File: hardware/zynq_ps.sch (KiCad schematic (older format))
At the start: 26 parts, among them J1801 DM3CS, SW1801 SW_Push, U1801 CAT24C02TDI-GT3, U1802 EMIF06-MSD02N16, U1803 33.333MHZ, U201 xc7z030sbg485

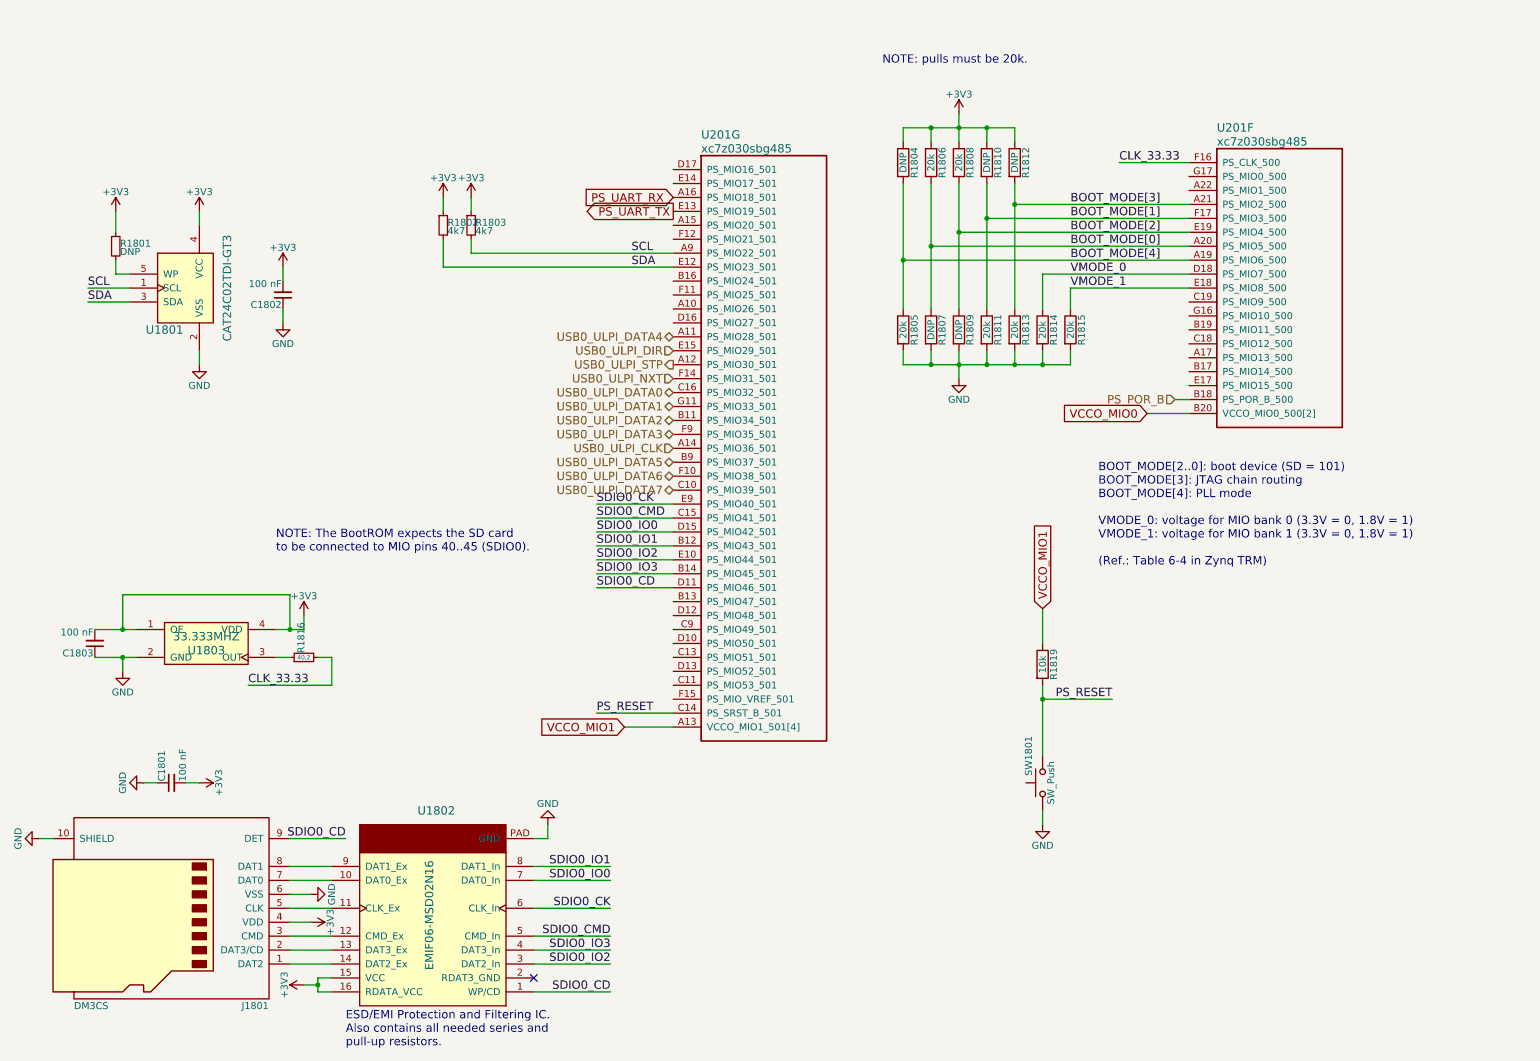
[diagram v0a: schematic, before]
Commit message: WIP: routing the HF Part of the Camera Connector. I have to move the clock away from the left border.
TODO: Fix DDR3 RAM.
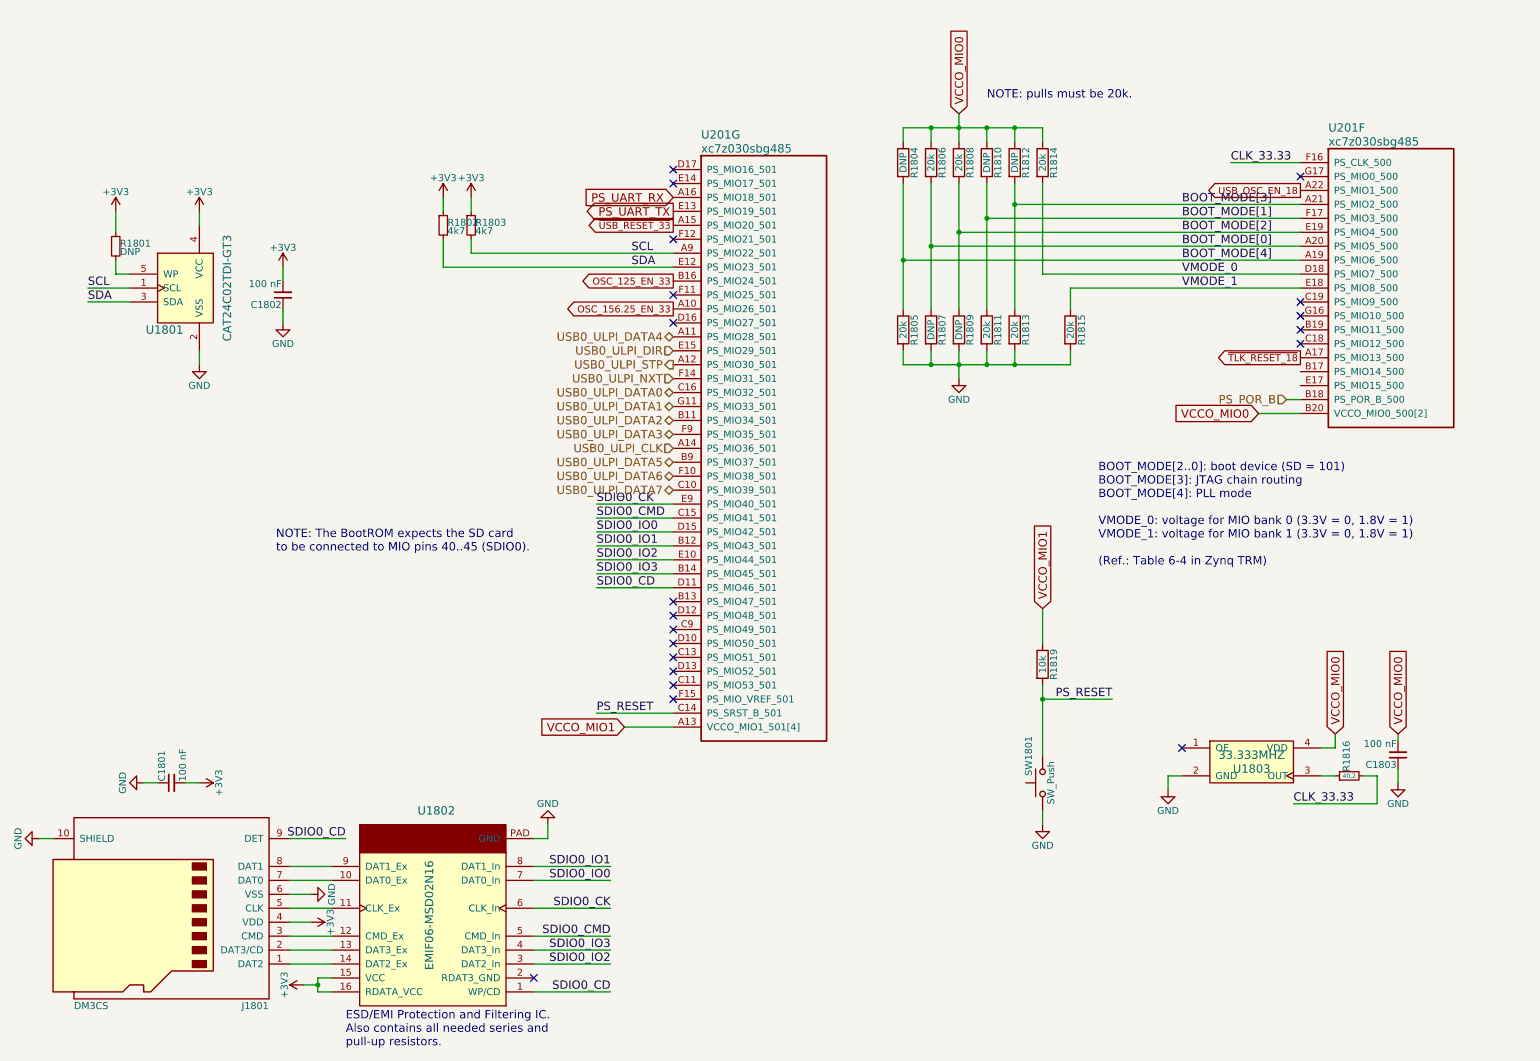
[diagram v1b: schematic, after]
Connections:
- net +3V3: no longer C1803.2, R1804.1, R1806.1, R1808.1, R1810.1, R1812.1, U1803.1 (OE), U1803.4 (VDD)
- net GND: no longer R1814.2
- net VCCO_MIO0: now also C1803.2, R1804.1, R1806.1, R1808.1, R1810.1, R1812.1, R1814.1, U1803.4 (VDD)
- net VMODE_0: now also R1814.2; no longer R1814.1
- net ~TLK_RESET_18~: now reaches U201.A17 (PS_MIO13_500)
- net USB_OSC_EN_18: now reaches U201.A22 (PS_MIO1_500)
- net OSC_156.25_EN_33: now reaches U201.A10 (PS_MIO26_501)
- net ~USB_RESET_33~: now reaches U201.A15 (PS_MIO20_501)
- net OSC_125_EN_33: now reaches U201.B16 (PS_MIO24_501)
- no-connect marks 1 -> 20
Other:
- moved on the sheet: C1803, R1814, R1816, U1803, U201F

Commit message: WIP: general Routing
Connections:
- net +3V3: no longer C1802.2, R1801.1, R1802.1, R1803.1, U1801.4 (VCC)
- net OSC_125_EN_33: now also U201.D10 (PS_MIO50_501); no longer U201.B16 (PS_MIO24_501)
- net OSC_156.25_EN_33: now also U201.C9 (PS_MIO49_501); no longer U201.A10 (PS_MIO26_501)
- net SCL: now also U201.C18 (PS_MIO12_500); no longer U201.A9 (PS_MIO22_501)
- net SDA: now also U201.A17 (PS_MIO13_500); no longer U201.E12 (PS_MIO23_501)
- net USB_OSC_EN_18: now also U201.B17 (PS_MIO14_500); no longer U201.A22 (PS_MIO1_500)
- net ~TLK_RESET_18~: now also U201.B19 (PS_MIO11_500); no longer U201.A17 (PS_MIO13_500)
- net CLK_SEL: now reaches U201.D12 (PS_MIO48_501)
- new net +1V8: C1802.2, R1801.1, R1802.1, R1803.1, U1801.4 (VCC)
- no-connect marks 20 -> 15
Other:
- moved on the sheet: R1802, R1803
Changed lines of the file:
@@
 $Descr A4 11693 8268
 encoding utf-8
-Sheet 16 21
+Sheet 14 21
 Title ""
 Date ""
@@
 $EndComp
 $Comp
-L power:+3V3 #PWR0235
-U 1 1 5ADF17FE
-P 2700 2150
-F 0 "#PWR0235" H 2700 2000 50  0001 C CNN
-F 1 "+3V3" H 2700 2290 50  0000 C CNN
-F 2 "" H 2700 2150 50  0001 C CNN
-F 3 "" H 2700 2150 50  0001 C CNN
-	1    2700 2150
-	1    0    0    -1
-$EndComp
-$Comp
 L Device:R_Small R1801
 U 1 1 5ADF2073
@@
 	1    0    0    -1
 $EndComp
-$Comp
-L power:+3V3 #PWR0236
-U 1 1 5ADF21D6
-P 1500 1750
-F 0 "#PWR0236" H 1500 1600 50  0001 C CNN
-F 1 "+3V3" H 1500 1890 50  0000 C CNN
-F 2 "" H 1500 1750 50  0001 C CNN
-F 3 "" H 1500 1750 50  0001 C CNN
-	1    1500 1750
-	1    0    0    -1
-$EndComp
 Text Label 1300 2300 0    60   ~ 0
 SCL
@@
 	1    0    0    -1
 $EndComp
-$Comp
-L power:+3V3 #PWR0238
-U 1 1 5ADF2B75
-P 2100 1750
-F 0 "#PWR0238" H 2100 1600 50  0001 C CNN
-F 1 "+3V3" H 2100 1890 50  0000 C CNN
-F 2 "" H 2100 1750 50  0001 C CNN
-F 3 "" H 2100 1750 50  0001 C CNN
-	1    2100 1750
-	1    0    0    -1
-$EndComp
-Text Label 5200 2050 0    60   ~ 0
+Text Label 9200 2700 0    60   ~ 0
 SCL
-Text Label 5200 2150 0    60   ~ 0
+Text Label 9200 2800 0    60   ~ 0
 SDA
 $Comp
 L Device:R_Small R1802
 U 1 1 5ADF492A
-P 3850 1850
-F 0 "R1802" H 3880 1870 50  0000 L CNN
-F 1 "4k7" H 3880 1810 50  0000 L CNN
-F 2 "Resistor_SMD:R_0402_1005Metric" H 3850 1850 50  0001 C CNN
-F 3 "" H 3850 1850 50  0001 C CNN
-F 4 "1" H 3850 1850 60  0001 C CNN "Populated"
-F 5 "SPEC" H 3850 1850 60  0001 C CNN "Source"
-F 6 "1" H 3850 1850 50  0001 C CNN "Populate for SBGA485(Z-7030)"
-F 7 "1" H 3850 1850 50  0001 C CNN "Populate for CLG484(Z-7012s/Z-7015)"
-	1    3850 1850
-	1    0    0    -1
-$EndComp
-$Comp
-L power:+3V3 #PWR0239
-U 1 1 5ADF4931
-P 3850 1650
-F 0 "#PWR0239" H 3850 1500 50  0001 C CNN
-F 1 "+3V3" H 3850 1790 50  0000 C CNN
-F 2 "" H 3850 1650 50  0001 C CNN
-F 3 "" H 3850 1650 50  0001 C CNN
-	1    3850 1650
-	1    0    0    -1
+P 8950 2800
+F 0 "R1802" H 8980 2820 50  0000 L CNN
+F 1 "4k7" H 8980 2760 50  0000 L CNN
+F 2 "Resistor_SMD:R_0402_1005Metric" H 8950 2800 50  0001 C CNN
+F 3 "" H 8950 2800 50  0001 C CNN
+F 4 "1" H 8950 2800 60  0001 C CNN "Populated"
+F 5 "SPEC" H 8950 2800 60  0001 C CNN "Source"
+F 6 "1" H 8950 2800 50  0001 C CNN "Populate for SBGA485(Z-7030)"
+F 7 "1" H 8950 2800 50  0001 C CNN "Populate for CLG484(Z-7012s/Z-7015)"
+	1    8950 2800
+	0    -1   1    0
 $EndComp
 $Comp
 L Device:R_Small R1803
 U 1 1 5ADF4A40
-P 4050 1850
-F 0 "R1803" H 4080 1870 50  0000 L CNN
-F 1 "4k7" H 4080 1810 50  0000 L CNN
-F 2 "Resistor_SMD:R_0402_1005Metric" H 4050 1850 50  0001 C CNN
-F 3 "" H 4050 1850 50  0001 C CNN
-F 4 "1" H 4050 1850 60  0001 C CNN "Populated"
-F 5 "SPEC" H 4050 1850 60  0001 C CNN "Source"
-F 6 "1" H 4050 1850 50  0001 C CNN "Populate for SBGA485(Z-7030)"
-F 7 "1" H 4050 1850 50  0001 C CNN "Populate for CLG484(Z-7012s/Z-7015)"
-	1    4050 1850
-	1    0    0    -1
-$EndComp
-$Comp
-L power:+3V3 #PWR0240
-U 1 1 5ADF4A46
-P 4050 1650
-F 0 "#PWR0240" H 4050 1500 50  0001 C CNN
-F 1 "+3V3" H 4050 1790 50  0000 C CNN
-F 2 "" H 4050 1650 50  0001 C CNN
-F 3 "" H 4050 1650 50  0001 C CNN
-	1    4050 1650
-	1    0    0    -1
+P 8950 2700
+F 0 "R1803" H 8980 2720 50  0000 L CNN
+F 1 "4k7" H 8980 2660 50  0000 L CNN
+F 2 "Resistor_SMD:R_0402_1005Metric" H 8950 2700 50  0001 C CNN
+F 3 "" H 8950 2700 50  0001 C CNN
+F 4 "1" H 8950 2700 60  0001 C CNN "Populated"
+F 5 "SPEC" H 8950 2700 60  0001 C CNN "Source"
+F 6 "1" H 8950 2700 50  0001 C CNN "Populate for SBGA485(Z-7030)"
+F 7 "1" H 8950 2700 50  0001 C CNN "Populate for CLG484(Z-7012s/Z-7015)"
+	1    8950 2700
+	0    -1   -1   0
 $EndComp
 Wire Wire Line
@@
 	2100 1750 2100 1850
 Wire Wire Line
-	4050 2050 5500 2050
-Wire Wire Line
-	3850 2150 5500 2150
-Wire Wire Line
-	3850 1650 3850 1750
-Wire Wire Line
-	4050 1650 4050 1750
-Wire Wire Line
-	4050 2050 4050 1950
-Wire Wire Line
-	3850 2150 3850 1950
+	8800 2800 8850 2800
+Wire Wire Line
+	8800 2700 8850 2700
 $Comp
 L Switch:SW_Push SW1801
@@
 	1    0    0    -1
 $EndComp
-NoConn ~ 5500 1450
 NoConn ~ 5500 1550
 NoConn ~ 5500 1950
@@
 NoConn ~ 5500 2550
 NoConn ~ 5500 4550
-NoConn ~ 5500 4650
-NoConn ~ 5500 4750
-NoConn ~ 5500 4850
 NoConn ~ 5500 4950
 NoConn ~ 5500 5050
@@
 NoConn ~ 10000 2400
 NoConn ~ 10000 2500
-NoConn ~ 10000 2600
-NoConn ~ 10000 2700
 Text GLabel 10250 5500 1    60   Input ~ 0
 VCCO_MIO0
@@
 Text GLabel 5500 1850 0    50   Output ~ 0
 ~USB_RESET_33~
-Text GLabel 10000 2800 0    50   Output ~ 0
+Text GLabel 10000 2600 0    50   Output ~ 0
 ~TLK_RESET_18~
-Text GLabel 5500 2250 0    50   Output ~ 0
+Text GLabel 5500 4850 0    50   Output ~ 0
 OSC_125_EN_33
-Text GLabel 5500 2450 0    50   Output ~ 0
+Text GLabel 5500 4750 0    50   Output ~ 0
 OSC_156.25_EN_33
 Wire Wire Line
@@
 	8350 2300 8350 2450
 NoConn ~ 9150 5600
-Text GLabel 10000 1600 0    50   Output ~ 0
+Text GLabel 10000 2900 0    50   Output ~ 0
 USB_OSC_EN_18
+NoConn ~ 5500 1450
+Text GLabel 5500 4650 0    50   Output ~ 0
+CLK_SEL
+$Comp
+L power:+1V8 #PWR0236
+U 1 1 5B52C316
+P 1500 1750
+F 0 "#PWR0236" H 1500 1600 50  0001 C CNN
+F 1 "+1V8" H 1515 1923 50  0000 C CNN
+F 2 "" H 1500 1750 50  0001 C CNN
+F 3 "" H 1500 1750 50  0001 C CNN
+	1    1500 1750
+	1    0    0    -1
+$EndComp
+$Comp
+L power:+1V8 #PWR0238
+U 1 1 5B52C379
+P 2100 1750
+F 0 "#PWR0238" H 2100 1600 50  0001 C CNN
+F 1 "+1V8" H 2115 1923 50  0000 C CNN
+F 2 "" H 2100 1750 50  0001 C CNN
+F 3 "" H 2100 1750 50  0001 C CNN
+	1    2100 1750
+	1    0    0    -1
+$EndComp
+$Comp
+L power:+1V8 #PWR0239
+U 1 1 5B52C3BA
+P 8800 2800
+F 0 "#PWR0239" H 8800 2650 50  0001 C CNN
+F 1 "+1V8" H 8815 2973 50  0000 C CNN
+F 2 "" H 8800 2800 50  0001 C CNN
+F 3 "" H 8800 2800 50  0001 C CNN
+	1    8800 2800
+	0    -1   1    0
+$EndComp
+$Comp
+L power:+1V8 #PWR0240
+U 1 1 5B52C3FB
+P 8800 2700
+F 0 "#PWR0240" H 8800 2550 50  0001 C CNN
+F 1 "+1V8" H 8815 2873 50  0000 C CNN
+F 2 "" H 8800 2700 50  0001 C CNN
+F 3 "" H 8800 2700 50  0001 C CNN
+	1    8800 2700
+	0    -1   -1   0
+$EndComp
+Wire Wire Line
+	9050 2700 10000 2700
+Wire Wire Line
+	9050 2800 10000 2800
+$Comp
+L power:+1V8 #PWR0235
+U 1 1 5B56238B
+P 2700 2150
+F 0 "#PWR0235" H 2700 2000 50  0001 C CNN
+F 1 "+1V8" H 2715 2323 50  0000 C CNN
+F 2 "" H 2700 2150 50  0001 C CNN
+F 3 "" H 2700 2150 50  0001 C CNN
+	1    2700 2150
+	1    0    0    -1
+$EndComp
 $EndSCHEMATC

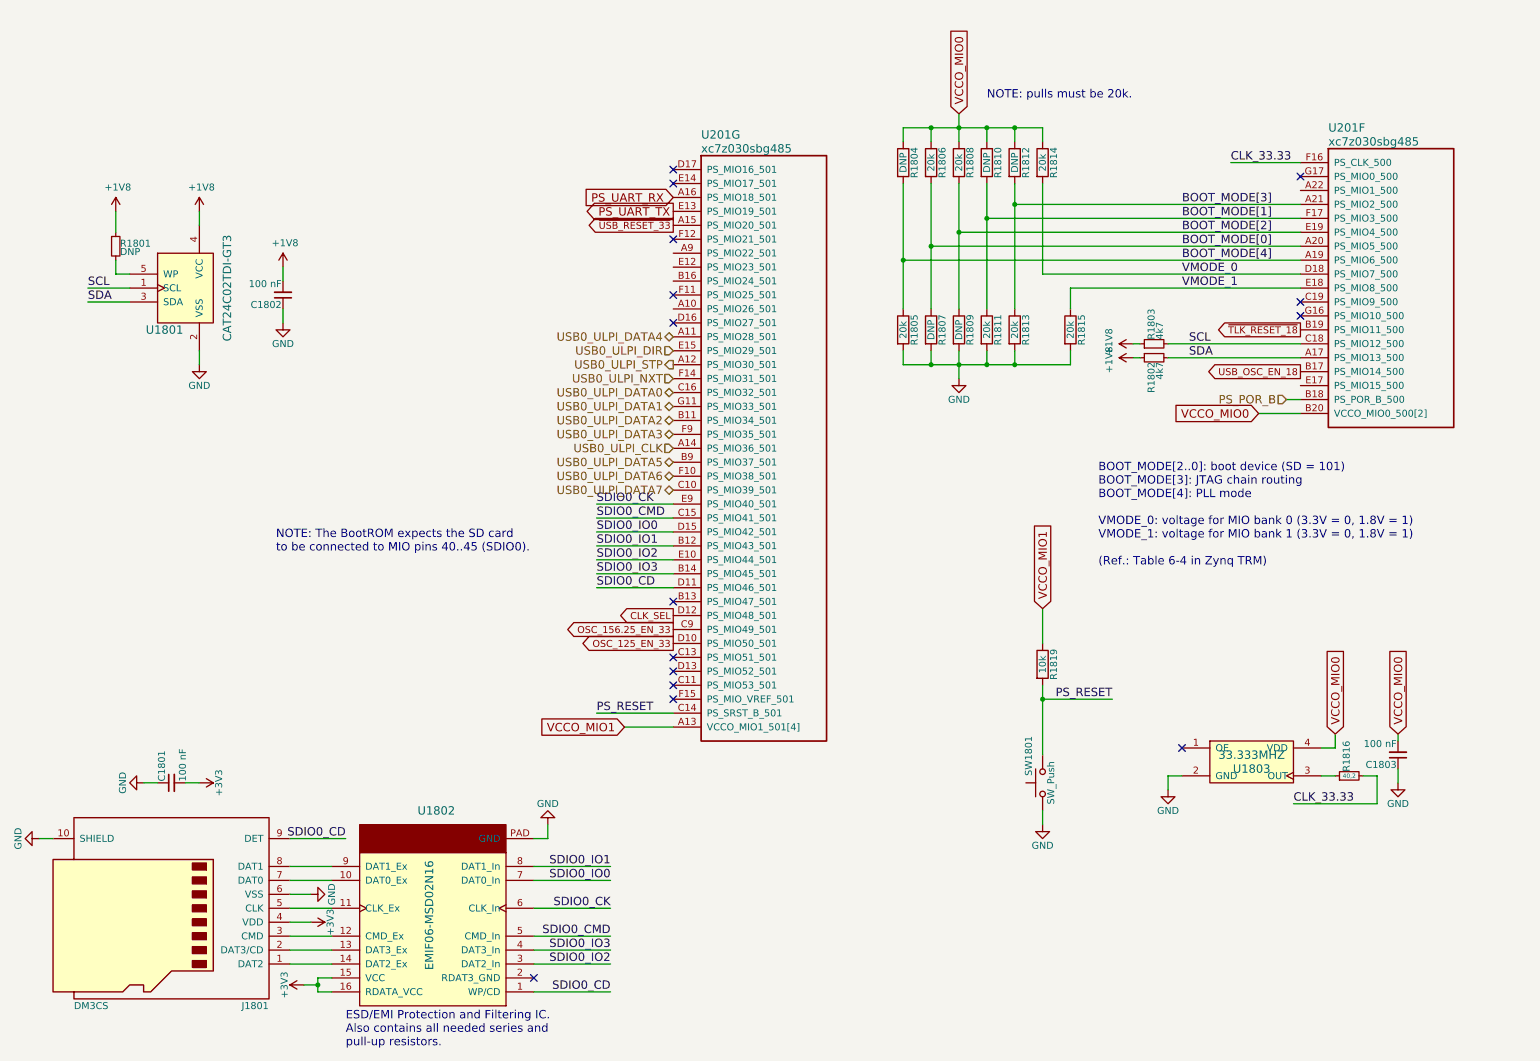
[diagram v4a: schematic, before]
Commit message: Routed extra GPIO Solder Pads, reannotated the whole schematic to make it consistent.
Power Distribution routing WIP
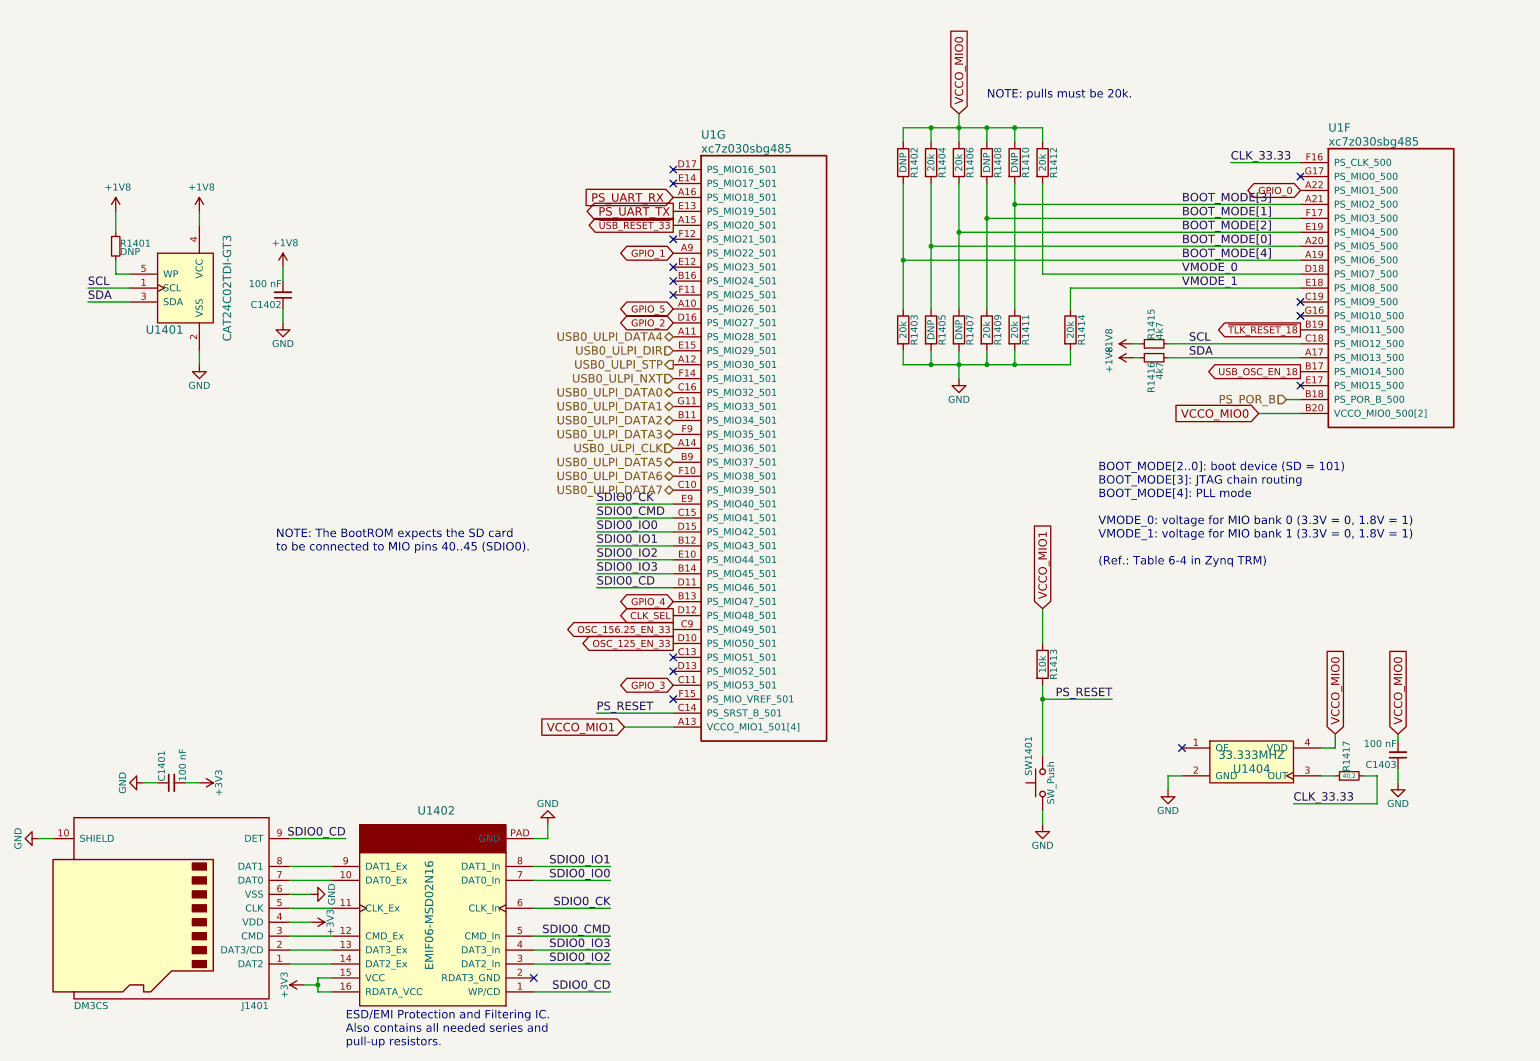
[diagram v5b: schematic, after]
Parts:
- U1: renamed from U201; Populate for CLG484(Z-7012s/Z-7015) (none) -> 1; Populate for SBGA485(Z-7030) (none) -> 1; Populated (none) -> 1; Source (none) -> SPEC
- renumbered C1801 to C1401, C1802 to C1402, C1803 to C1403, J1801 to J1401, R1801 to R1401, R1804 to R1402, R1805 to R1403, R1806 to R1404, R1807 to R1405, R1808 to R1406, R1809 to R1407, R1810 to R1408, R1811 to R1409, R1812 to R1410, R1813 to R1411, R1814 to R1412, R1819 to R1413, R1815 to R1414, R1803 to R1415, R1802 to R1416, R1816 to R1417, SW1801 to SW1401, U1801 to U1401, U1802 to U1402, U1803 to U1404
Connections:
- net GPIO_0: now reaches U1.A22 (PS_MIO1_500)
- net GPIO_5: now reaches U1.A10 (PS_MIO26_501)
- net GPIO_1: now reaches U1.A9 (PS_MIO22_501)
- net GPIO_4: now reaches U1.B13 (PS_MIO47_501)
- net GPIO_3: now reaches U1.C11 (PS_MIO53_501)
- net GPIO_2: now reaches U1.D16 (PS_MIO27_501)

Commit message: general routing mainly power distribution, fixed some footprints
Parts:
- R1401: footprint Resistors_SMD:R_0603 -> Resistor_SMD:R_0603_1608Metric
- U1401: footprint TO_SOT_Packages_SMD:SOT-23-5 -> Package_TO_SOT_SMD:SOT-23-5
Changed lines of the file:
@@
 F 0 "U1401" H 1850 2000 60  0000 C CNN
 F 1 "CAT24C02TDI-GT3" V 2300 2300 60  0000 C CNN
-F 2 "TO_SOT_Packages_SMD:SOT-23-5" H 2800 1450 60  0001 C CNN
+F 2 "Package_TO_SOT_SMD:SOT-23-5" H 2800 1450 60  0001 C CNN
 F 3 "http://www.onsemi.com/pub/Collateral/CAT24C01-D.PDF" H 2800 1450 60  0001 C CNN
 F 4 "ON Semiconductor" H 2100 2300 60  0001 C CNN "MFG Name"
@@
 F 0 "R1401" H 1530 2020 50  0000 L CNN
 F 1 "DNP" H 1530 1960 50  0000 L CNN
-F 2 "Resistors_SMD:R_0603" H 1500 2000 50  0001 C CNN
+F 2 "Resistor_SMD:R_0603_1608Metric" H 1500 2000 50  0001 C CNN
 F 3 "" H 1500 2000 50  0001 C CNN
 F 4 "0" H 1500 2000 60  0001 C CNN "Populated"
